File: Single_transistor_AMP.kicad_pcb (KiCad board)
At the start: 2 copper layers, 0 parts

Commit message: Set design rules, created PCB layout and traces, positioned labels
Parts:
- added C1: 1uF, Capacitor_THT:C_Disc_D4.3mm_W1.9mm_P5.00mm, F.Cu at (159.5, 114.6)
- added C2: 2uF, Capacitor_THT:C_Disc_D4.7mm_W2.5mm_P5.00mm, F.Cu at (156.7, 119.6)
- added J1: 9V_IN, TerminalBlock:TerminalBlock_bornier-2_P5.08mm, F.Cu at (148.8, 124.7)
- added J2: SIG_OUT, TerminalBlock:TerminalBlock_bornier-2_P5.08mm, F.Cu at (149.6, 103.8)
- added J3: SIG_IN, TerminalBlock:TerminalBlock_bornier-2_P5.08mm, F.Cu at (154.4, 124.7)
- added Q1: BC547, Package_TO_SOT_THT:TO-92_Inline, F.Cu at (156.7, 111.8)
- added R1: 4.7k, Resistor_THT:R_Axial_DIN0207_L6.3mm_D2.5mm_P10.16mm_Horizontal, F.Cu at (142.7, 119.6)
- added R2: 4.7k, Resistor_THT:R_Axial_DIN0207_L6.3mm_D2.5mm_P10.16mm_Horizontal, F.Cu at (145.8, 119.6)
- added R3: 1k, Resistor_THT:R_Axial_DIN0207_L6.3mm_D2.5mm_P10.16mm_Horizontal, F.Cu at (148.8, 109.5)
- added R4: 1k, Resistor_THT:R_Axial_DIN0207_L6.3mm_D2.5mm_P10.16mm_Horizontal, F.Cu at (151.9, 109.5)
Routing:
- net Net-(C1-Pad1): track 0.00 -> 20.6 mm
- net Net-(J2-Pad2): track 0.00 -> 19.0 mm
- net Net-(C2-Pad2): track 0.00 -> 8.84 mm
- net Net-(J1-Pad2): track 0.00 -> 8.60 mm
- net Net-(C1-Pad2): track 0.00 -> 5.21 mm
- added copper zone on B.Cu, net GND
- added copper zone on F.Cu, net GND
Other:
- board outline added: 22.4 x 30 mm
- net class Default: trace_width 0.25 -> 0.2
- net class Power: clearance 0.5 -> 0.4
- net class Signal added: clearance 0.2, trace_width 0.3, via_dia 0.8, via_drill 0.4

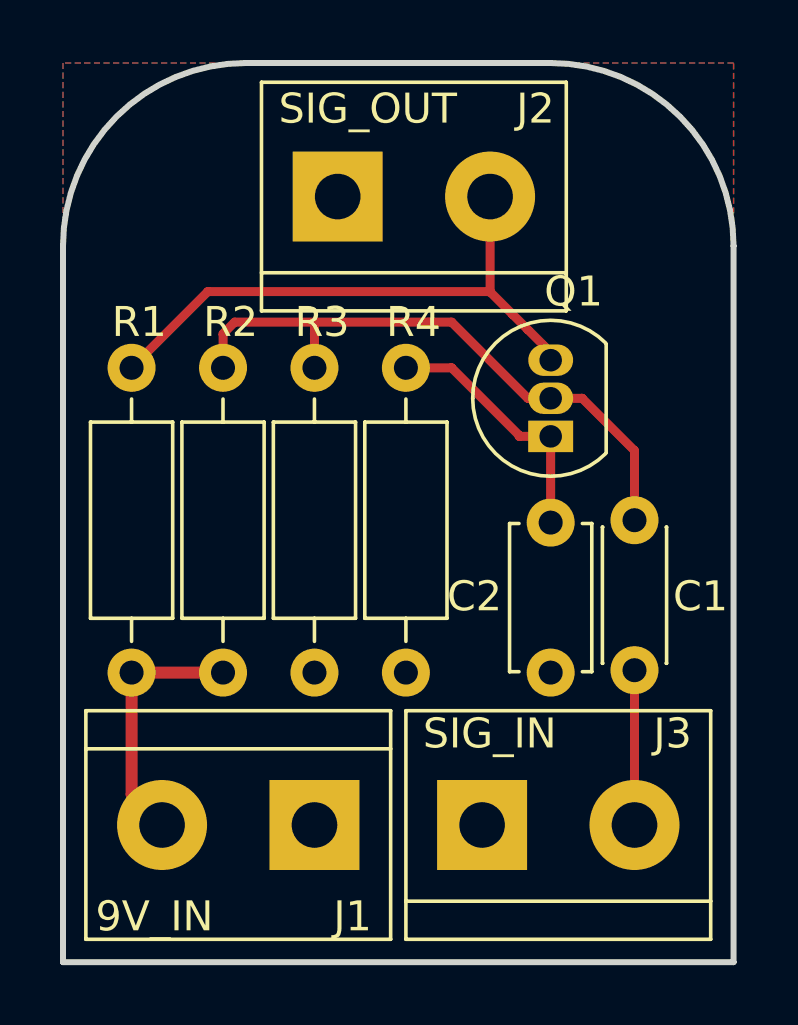
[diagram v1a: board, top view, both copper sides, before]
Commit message: Fixed a DRC issue, improved traces
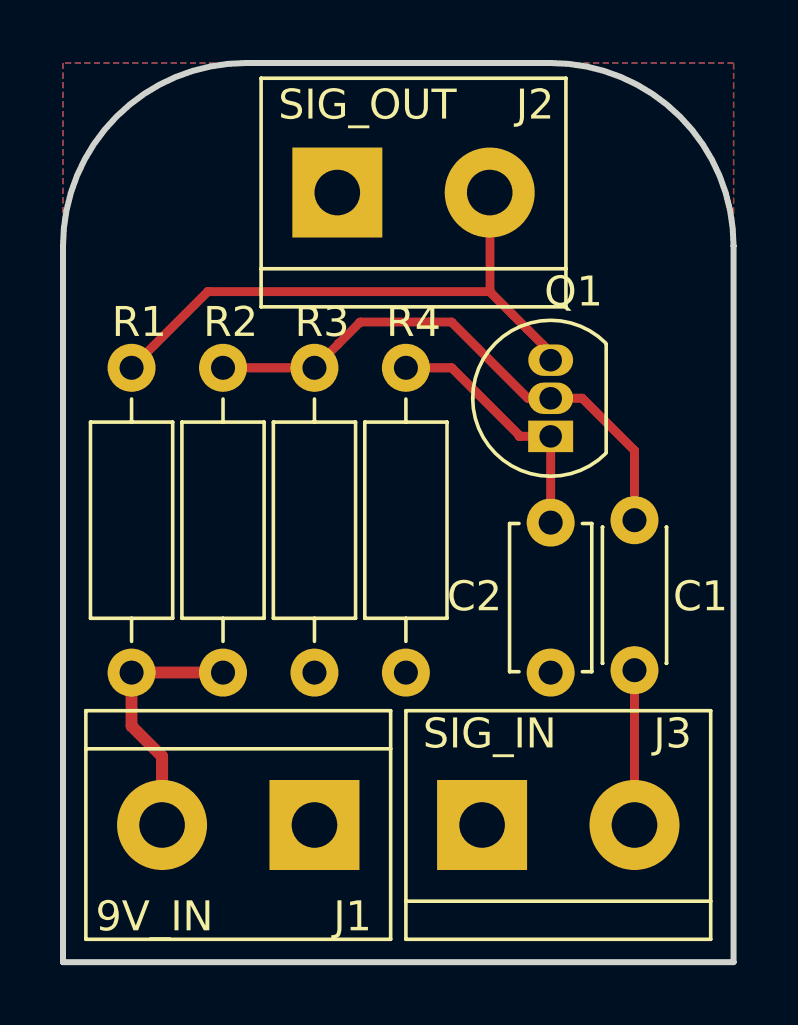
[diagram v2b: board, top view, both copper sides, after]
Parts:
- moved J2 0.13 mm to (149.6, 103.6)
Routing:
- net Net-(C1-Pad1): track 20.6 -> 18.4 mm
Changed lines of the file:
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@@
     (thickness 1.6)
     (drawings 6)
-    (tracks 32)
+    (tracks 31)
     (zones 0)
     (modules 10)
@@
   )
   (module TerminalBlock:TerminalBlock_bornier-2_P5.08mm (layer F.Cu)
-    (at 149.618 103.766)
+    (at 149.606 103.632)
     (descr "simple 2-pin terminal block, pitch 5.08mm, revamped version of bornier2")
     (tags "terminal block bornier2")
@@
   (gr_line (start 162.814 129.286) (end 162.814 105.41) (layer Edge.Cuts) (width 0.2))
   (gr_line (start 140.462 129.286) (end 162.814 129.286) (layer Edge.Cuts) (width 0.2))
-  (segment (start 145.796 108.34263) (end 146.18863 107.95) (width 0.3) (layer F.Cu) (net 1))
-  (segment (start 145.796 109.474) (end 145.796 108.34263) (width 0.3) (layer F.Cu) (net 1))
-  (segment (start 148.844 108.34263) (end 148.844 107.95) (width 0.3) (layer F.Cu) (net 1))
-  (segment (start 148.844 109.474) (end 148.844 108.34263) (width 0.3) (layer F.Cu) (net 1))
-  (segment (start 146.18863 107.95) (end 148.844 107.95) (width 0.3) (layer F.Cu) (net 1))
   (segment (start 159.512 112.234) (end 159.512 113.42263) (width 0.3) (layer F.Cu) (net 1))
   (segment (start 156.718 110.49) (end 157.768 110.49) (width 0.3) (layer F.Cu) (net 1))
   (segment (start 157.768 110.49) (end 159.512 112.234) (width 0.3) (layer F.Cu) (net 1))
   (segment (start 159.512 113.42263) (end 159.512 114.554) (width 0.3) (layer F.Cu) (net 1))
-  (segment (start 152.654 107.95) (end 148.844 107.95) (width 0.3) (layer F.Cu) (net 1))
   (segment (start 153.416 107.95) (end 152.654 107.95) (width 0.3) (layer F.Cu) (net 1))
   (segment (start 156.718 110.49) (end 155.956 110.49) (width 0.3) (layer F.Cu) (net 1))
   (segment (start 155.956 110.49) (end 153.416 107.95) (width 0.3) (layer F.Cu) (net 1))
+  (segment (start 145.796 109.474) (end 148.844 109.474) (width 0.3) (layer F.Cu) (net 1))
+  (segment (start 149.643999 108.674001) (end 150.368 107.95) (width 0.3) (layer F.Cu) (net 1))
+  (segment (start 148.844 109.474) (end 149.643999 108.674001) (width 0.3) (layer F.Cu) (net 1))
+  (segment (start 152.654 107.95) (end 150.368 107.95) (width 0.3) (layer F.Cu) (net 1))
   (segment (start 159.512 124.714) (end 159.512 119.507) (width 0.3) (layer F.Cu) (net 2))
   (segment (start 156.718 111.76) (end 156.718 114.808) (width 0.3) (layer F.Cu) (net 3))
@@
   (segment (start 153.416 109.474) (end 155.668 111.726) (width 0.3) (layer F.Cu) (net 3))
   (segment (start 143.764 124.766) (end 143.764 124.714) (width 0.4) (layer F.Cu) (net 4))
-  (segment (start 143.764 124.714) (end 142.875 123.825) (width 0.4) (layer F.Cu) (net 4))
-  (segment (start 142.875 123.825) (end 142.748 123.698) (width 0.4) (layer F.Cu) (net 4))
-  (segment (start 142.748 123.698) (end 142.748 119.634) (width 0.4) (layer F.Cu) (net 4))
   (segment (start 142.748 119.634) (end 145.796 119.634) (width 0.4) (layer F.Cu) (net 4))
+  (segment (start 143.764 124.714) (end 143.764 122.59268) (width 0.4) (layer F.Cu) (net 4))
+  (segment (start 143.764 122.59268) (end 143.764 122.428) (width 0.4) (layer F.Cu) (net 4))
+  (segment (start 143.764 122.428) (end 142.748 121.412) (width 0.4) (layer F.Cu) (net 4))
+  (segment (start 142.748 121.412) (end 142.748 119.634) (width 0.4) (layer F.Cu) (net 4))
   (segment (start 142.748 109.474) (end 145.288 106.934) (width 0.3) (layer F.Cu) (net 6))
   (segment (start 154.698 106.922) (end 154.686 106.934) (width 0.3) (layer F.Cu) (net 6))
